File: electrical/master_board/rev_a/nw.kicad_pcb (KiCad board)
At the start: 2 copper layers, 42.2 x 39 mm, 1 part, among them CN70 HCSR04;F1x4H

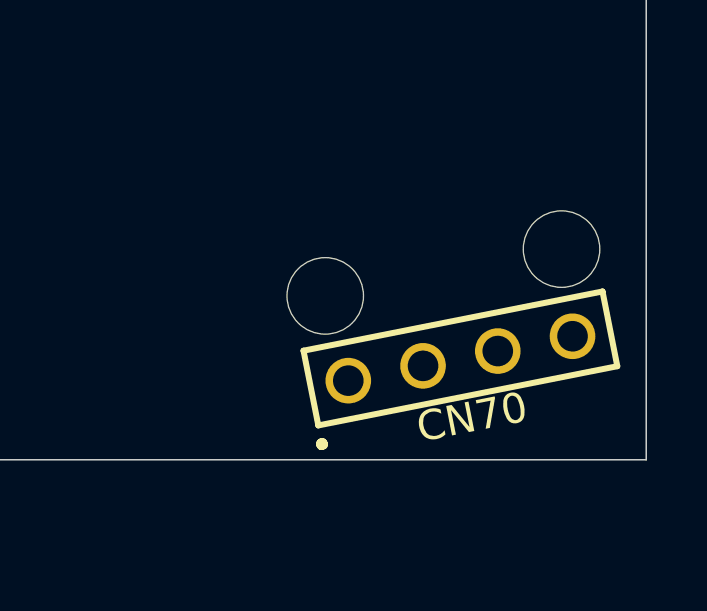
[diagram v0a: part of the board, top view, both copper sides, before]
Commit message: The PCBChunk'ification of Sonars is complete.
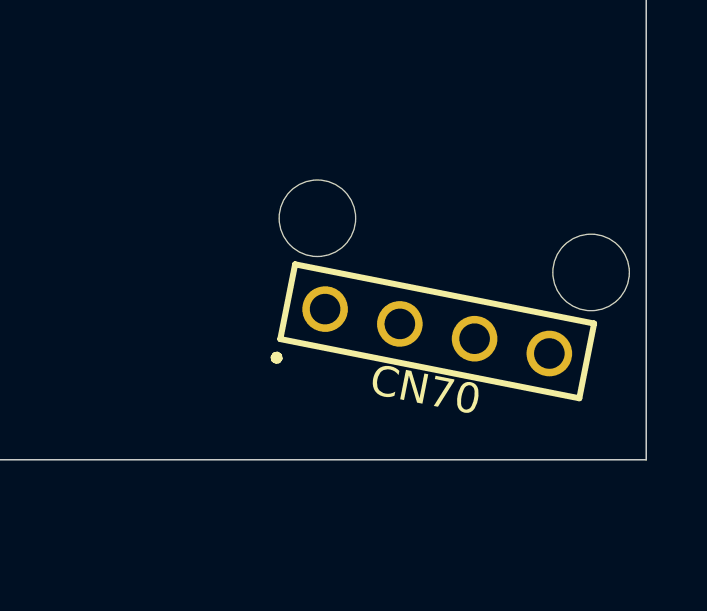
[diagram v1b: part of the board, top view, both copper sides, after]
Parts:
- CN70: value HCSR04;F1x4H -> HCSR04H;F1X4
- moved CN70 1.19 mm to (63.0, 56.7), turned to 168.8 degrees
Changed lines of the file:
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@@
   )
   (module HR2:HCSR04_F1x4H (layer F.Cu)
-    (at 63.8063 57.6226 191.2)
-    (fp_text reference CN70 (at 0 -2 11.2) (layer F.SilkS)
+    (at 63.0334 56.7177 168.8)
+    (fp_text reference CN70 (at 0 -2 168.8) (layer F.SilkS)
       (effects (font (size 1 1) (thickness 0.2)))
     )
-    (fp_text value HCSR04;F1x4H (at 0 0 11.2) (layer F.Fab)
+    (fp_text value HCSR04H;F1X4 (at 0 0 168.8) (layer F.Fab)
       (effects (font (size 1 1) (thickness 0.2)))
     )
@@
     (fp_line (start -5.08 1.27) (end -5.08 -1.27) (layer F.SilkS) (width 0.2))
     (fp_line (start -5.08 -1.27) (end 5.08 -1.27) (layer F.SilkS) (width 0.2))
-    (pad "HCSR04 West Tie Down Hole (High)" np_thru_hole circle (at -4.015 2.921 191.2) (size 2.55 2.55) (drill 2.55) (layers *.Cu *.Mask))
-    (pad "HCSR04 East Tie Down Hole (Hight)" np_thru_hole circle (at 4.015 2.921 191.2) (size 2.55 2.55) (drill 2.55) (layers *.Cu *.Mask))
-    (pad 4 thru_hole circle (at -3.81 0 191.2) (size 1.52 1.52) (drill 1.02) (layers *.Cu *.Mask))
-    (pad 3 thru_hole circle (at -1.27 0 191.2) (size 1.52 1.52) (drill 1.02) (layers *.Cu *.Mask))
-    (pad 2 thru_hole circle (at 1.27 0 191.2) (size 1.52 1.52) (drill 1.02) (layers *.Cu *.Mask))
-    (pad 1 thru_hole circle (at 3.81 0 191.2) (size 1.52 1.52) (drill 1.02) (layers *.Cu *.Mask))
+    (pad "HCSR04 West Tie Down Hole (High)" np_thru_hole circle (at -4.65 2.921 168.8) (size 2.55 2.55) (drill 2.55) (layers *.Cu *.Mask))
+    (pad "HCSR04 East Tie Down Hole (Hight)" np_thru_hole circle (at 4.65 2.921 168.8) (size 2.55 2.55) (drill 2.55) (layers *.Cu *.Mask))
+    (pad 4 thru_hole circle (at -3.81 0 168.8) (size 1.52 1.52) (drill 1.02) (layers *.Cu *.Mask))
+    (pad 3 thru_hole circle (at -1.27 0 168.8) (size 1.52 1.52) (drill 1.02) (layers *.Cu *.Mask))
+    (pad 2 thru_hole circle (at 1.27 0 168.8) (size 1.52 1.52) (drill 1.02) (layers *.Cu *.Mask))
+    (pad 1 thru_hole circle (at 3.81 0 168.8) (size 1.52 1.52) (drill 1.02) (layers *.Cu *.Mask))
   )
   (gr_line (start 70 61) (end 70 26.46) (layer Edge.Cuts) (width 0.05))

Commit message: Finally have everything fitting together.
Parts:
- moved CN70 3.97 mm to (61.9, 60.5)
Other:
- outline, holes or cut-outs redrawn
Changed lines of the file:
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@@
   )
   (module HR2:HCSR04_F1x4H (layer F.Cu)
-    (at 63.0334 56.7177 168.8)
+    (at 61.8716 60.5169 168.8)
     (fp_text reference CN70 (at 0 -2 168.8) (layer F.SilkS)
       (effects (font (size 1 1) (thickness 0.2)))
@@
     (pad 1 thru_hole circle (at 3.81 0 168.8) (size 1.52 1.52) (drill 1.02) (layers *.Cu *.Mask))
   )
-  (gr_line (start 70 61) (end 70 26.46) (layer Edge.Cuts) (width 0.05))
+  (gr_line (start 70 61.5) (end 70 26.46) (layer Edge.Cuts) (width 0.05))
   (gr_line (start 70 26.46) (end 69.99 26.33) (layer Edge.Cuts) (width 0.05))
   (gr_line (start 69.99 26.33) (end 69.98 26.19) (layer Edge.Cuts) (width 0.05))
@@
   (gr_line (start 29.2 63.99) (end 29.33 64) (layer Edge.Cuts) (width 0.05))
   (gr_line (start 29.33 64) (end 37.5 64) (layer Edge.Cuts) (width 0.05))
-  (gr_line (start 37.5 64) (end 37.5 62.5) (layer Edge.Cuts) (width 0.05))
-  (gr_line (start 37.5 62.5) (end 37.51 62.37) (layer Edge.Cuts) (width 0.05))
-  (gr_line (start 37.51 62.37) (end 37.52 62.24) (layer Edge.Cuts) (width 0.05))
-  (gr_line (start 37.52 62.24) (end 37.55 62.11) (layer Edge.Cuts) (width 0.05))
-  (gr_line (start 37.55 62.11) (end 37.59 61.99) (layer Edge.Cuts) (width 0.05))
-  (gr_line (start 37.59 61.99) (end 37.64 61.87) (layer Edge.Cuts) (width 0.05))
-  (gr_line (start 37.64 61.87) (end 37.7 61.75) (layer Edge.Cuts) (width 0.05))
-  (gr_line (start 37.7 61.75) (end 37.77 61.64) (layer Edge.Cuts) (width 0.05))
-  (gr_line (start 37.77 61.64) (end 37.85 61.54) (layer Edge.Cuts) (width 0.05))
-  (gr_line (start 37.85 61.54) (end 37.94 61.44) (layer Edge.Cuts) (width 0.05))
-  (gr_line (start 37.94 61.44) (end 38.04 61.35) (layer Edge.Cuts) (width 0.05))
-  (gr_line (start 38.04 61.35) (end 38.14 61.27) (layer Edge.Cuts) (width 0.05))
-  (gr_line (start 38.14 61.27) (end 38.25 61.2) (layer Edge.Cuts) (width 0.05))
-  (gr_line (start 38.25 61.2) (end 38.37 61.14) (layer Edge.Cuts) (width 0.05))
-  (gr_line (start 38.37 61.14) (end 38.49 61.09) (layer Edge.Cuts) (width 0.05))
-  (gr_line (start 38.49 61.09) (end 38.61 61.05) (layer Edge.Cuts) (width 0.05))
-  (gr_line (start 38.61 61.05) (end 38.74 61.02) (layer Edge.Cuts) (width 0.05))
-  (gr_line (start 38.74 61.02) (end 38.87 61.01) (layer Edge.Cuts) (width 0.05))
-  (gr_line (start 38.87 61.01) (end 39 61) (layer Edge.Cuts) (width 0.05))
-  (gr_line (start 39 61) (end 70 61) (layer Edge.Cuts) (width 0.05))
+  (gr_line (start 37.5 64) (end 37.5 63) (layer Edge.Cuts) (width 0.05))
+  (gr_line (start 37.5 63) (end 37.51 62.87) (layer Edge.Cuts) (width 0.05))
+  (gr_line (start 37.51 62.87) (end 37.52 62.74) (layer Edge.Cuts) (width 0.05))
+  (gr_line (start 37.52 62.74) (end 37.55 62.61) (layer Edge.Cuts) (width 0.05))
+  (gr_line (start 37.55 62.61) (end 37.59 62.49) (layer Edge.Cuts) (width 0.05))
+  (gr_line (start 37.59 62.49) (end 37.64 62.37) (layer Edge.Cuts) (width 0.05))
+  (gr_line (start 37.64 62.37) (end 37.7 62.25) (layer Edge.Cuts) (width 0.05))
+  (gr_line (start 37.7 62.25) (end 37.77 62.14) (layer Edge.Cuts) (width 0.05))
+  (gr_line (start 37.77 62.14) (end 37.85 62.04) (layer Edge.Cuts) (width 0.05))
+  (gr_line (start 37.85 62.04) (end 37.94 61.94) (layer Edge.Cuts) (width 0.05))
+  (gr_line (start 37.94 61.94) (end 38.04 61.85) (layer Edge.Cuts) (width 0.05))
+  (gr_line (start 38.04 61.85) (end 38.14 61.77) (layer Edge.Cuts) (width 0.05))
+  (gr_line (start 38.14 61.77) (end 38.25 61.7) (layer Edge.Cuts) (width 0.05))
+  (gr_line (start 38.25 61.7) (end 38.37 61.64) (layer Edge.Cuts) (width 0.05))
+  (gr_line (start 38.37 61.64) (end 38.49 61.59) (layer Edge.Cuts) (width 0.05))
+  (gr_line (start 38.49 61.59) (end 38.61 61.55) (layer Edge.Cuts) (width 0.05))
+  (gr_line (start 38.61 61.55) (end 38.74 61.52) (layer Edge.Cuts) (width 0.05))
+  (gr_line (start 38.74 61.52) (end 38.87 61.51) (layer Edge.Cuts) (width 0.05))
+  (gr_line (start 38.87 61.51) (end 39 61.5) (layer Edge.Cuts) (width 0.05))
+  (gr_line (start 39 61.5) (end 70 61.5) (layer Edge.Cuts) (width 0.05))
 )

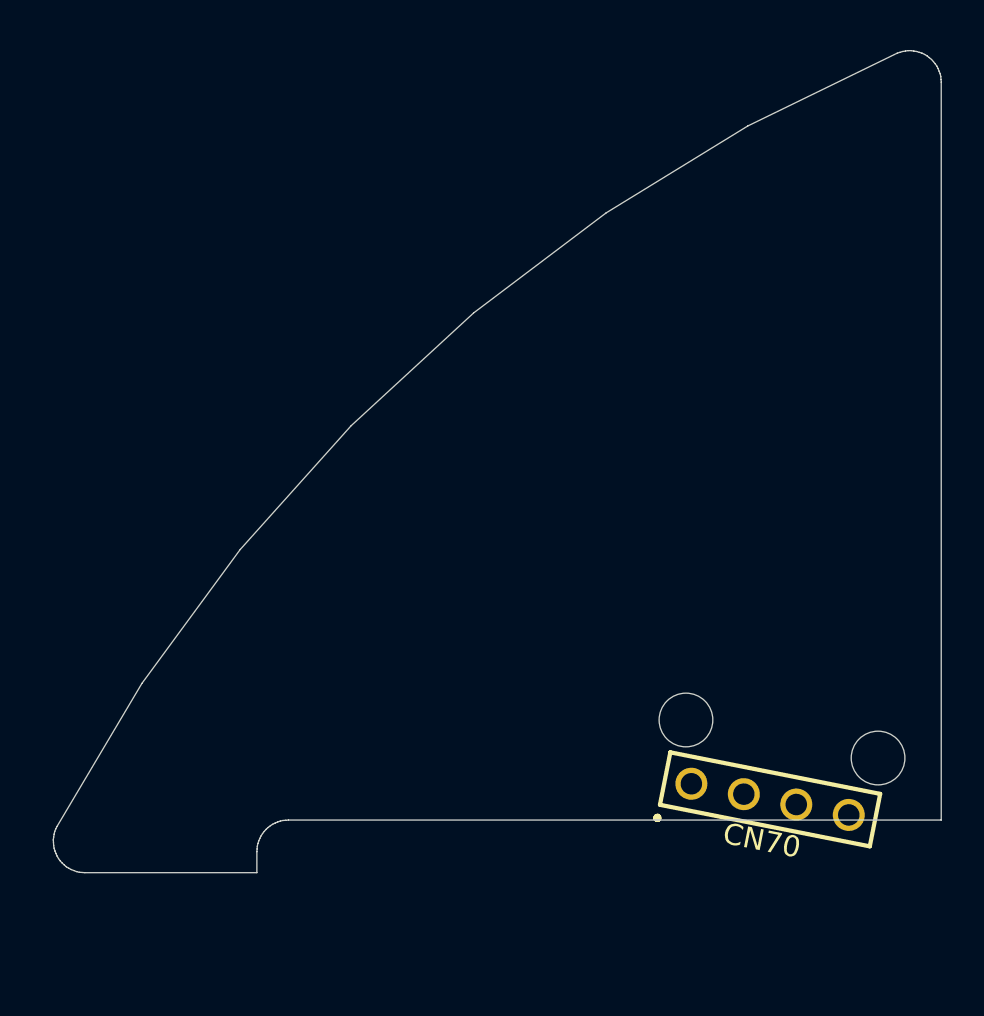
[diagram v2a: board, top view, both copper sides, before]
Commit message: Added spacer mounting holes to schematics and associated PCB's.
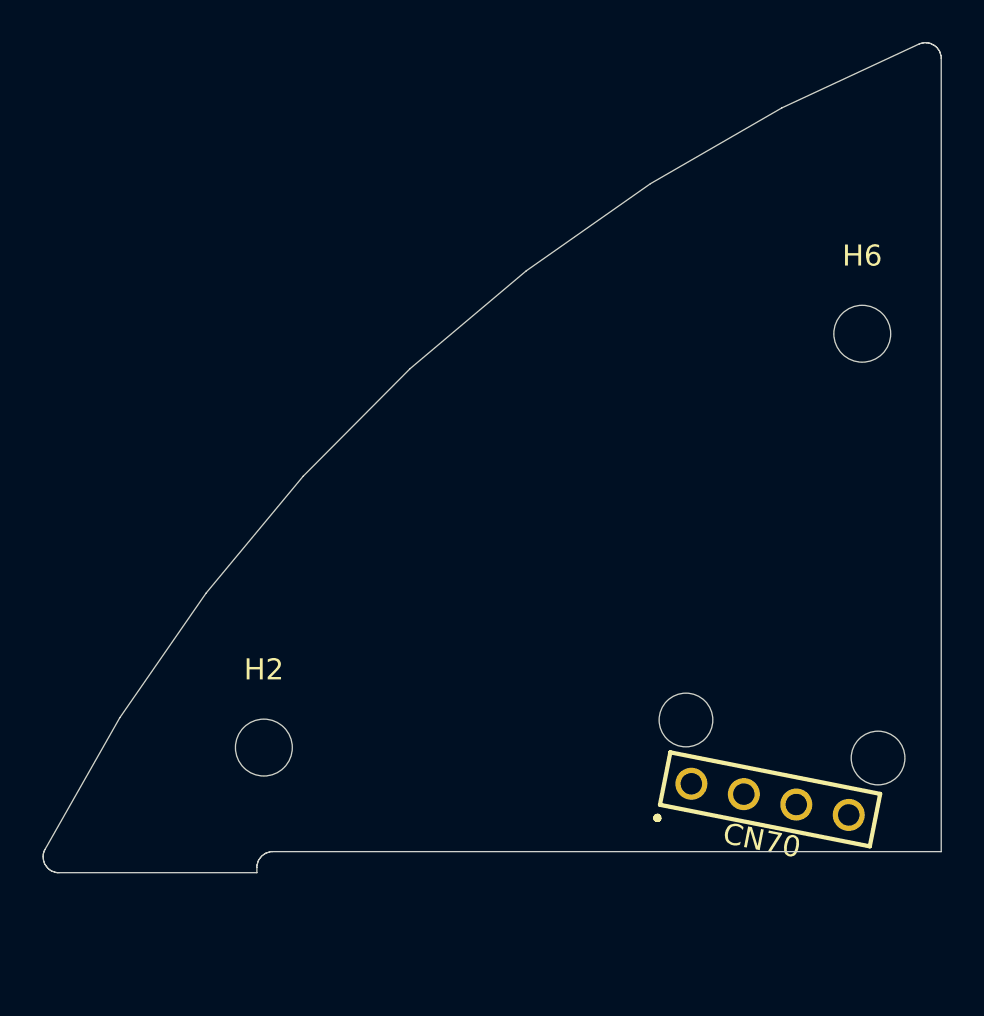
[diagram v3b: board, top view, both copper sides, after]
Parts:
- added H2: HOLE;M2.5, MountingHole:MountingHole_2.7mm_M2.5, F.Cu at (37.8, 58.1)
- added H6: HOLE;M2.5, MountingHole:MountingHole_2.7mm_M2.5, F.Cu at (66.2, 38.4)
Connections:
- CN70 pad 1: (no net) -> Net-(CN70-Pad1)
- CN70 pad 2: (no net) -> Net-(CN70-Pad2)
- CN70 pad 3: (no net) -> Net-(CN70-Pad3)
- CN70 pad 4: (no net) -> Net-(CN70-Pad4)
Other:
- board size 42.2 x 39 mm -> 42.6 x 39.4 mm

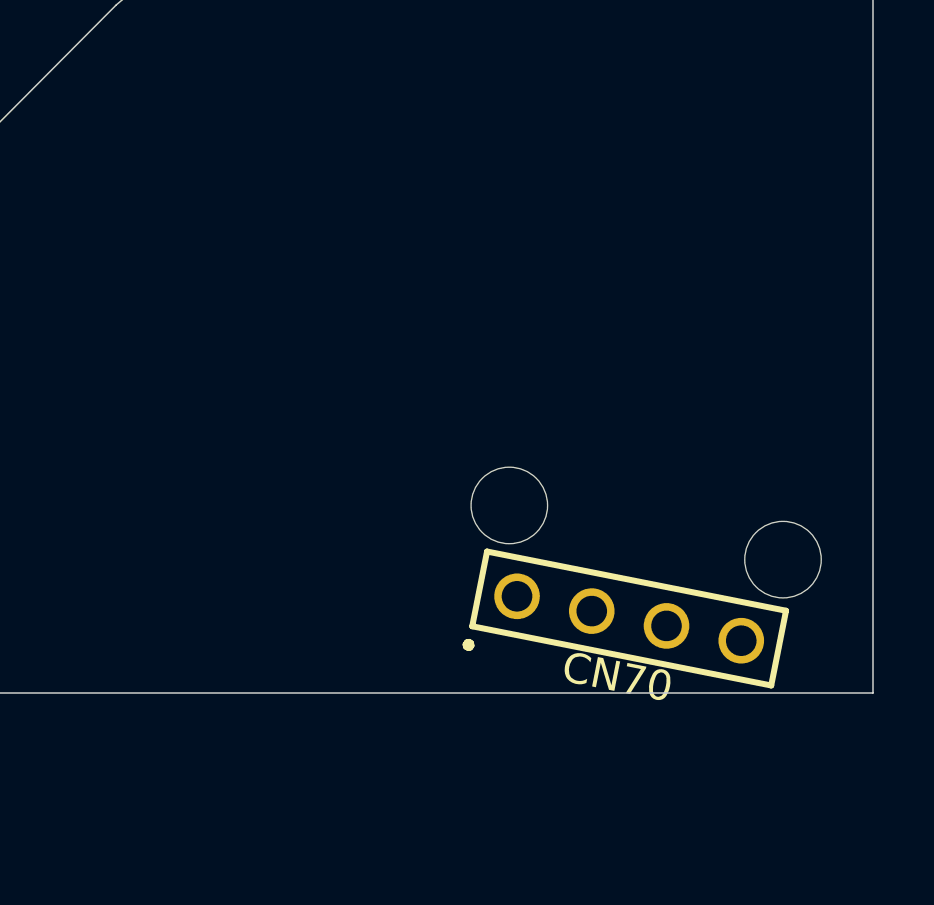
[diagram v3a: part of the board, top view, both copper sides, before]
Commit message: Placed all of the Groves on the PCB's.
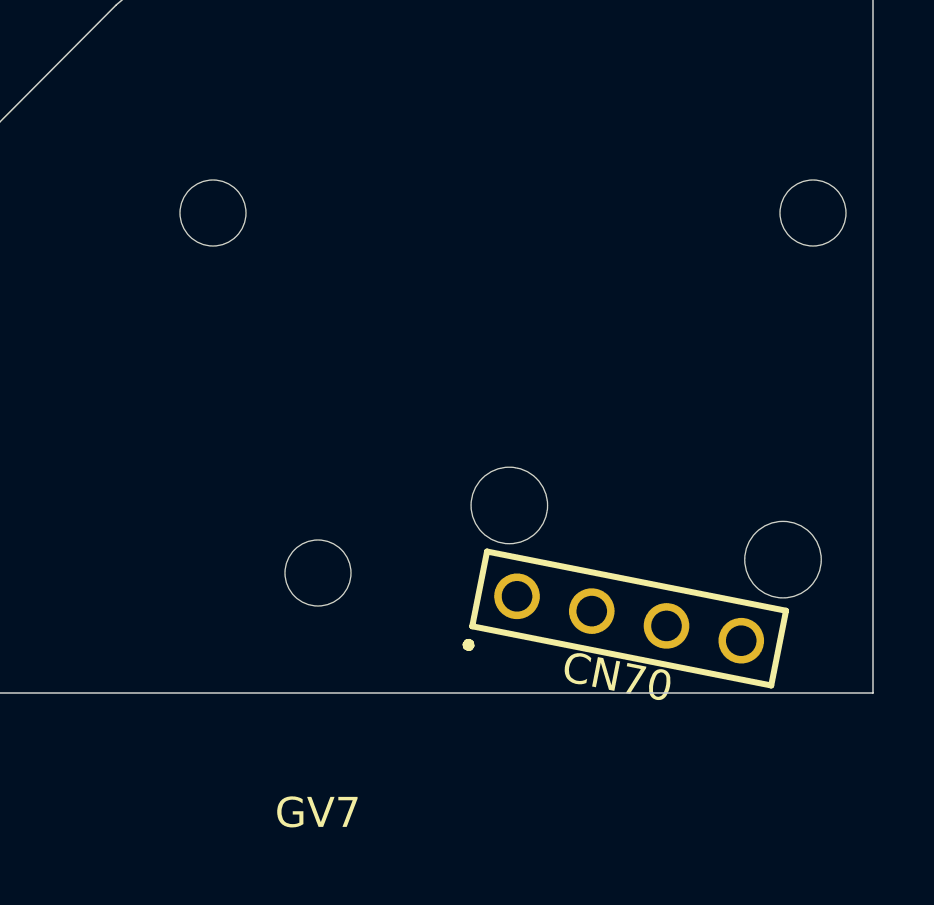
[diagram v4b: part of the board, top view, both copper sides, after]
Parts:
- added GV1: GROVE;20x20, HR2:GROVE20x20, B.Cu at (58.0, 47.0)
- added GV7: GROVE;20x20R, HR2:GROVE20x20R, F.Cu at (51.5, 69.0)

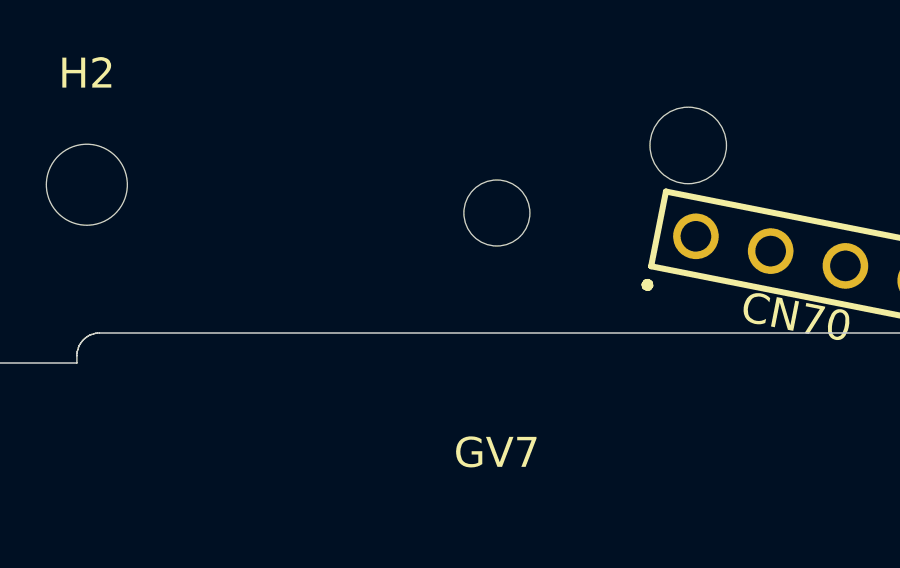
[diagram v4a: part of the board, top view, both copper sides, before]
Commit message: Fixed Groves and added MikroBus's.
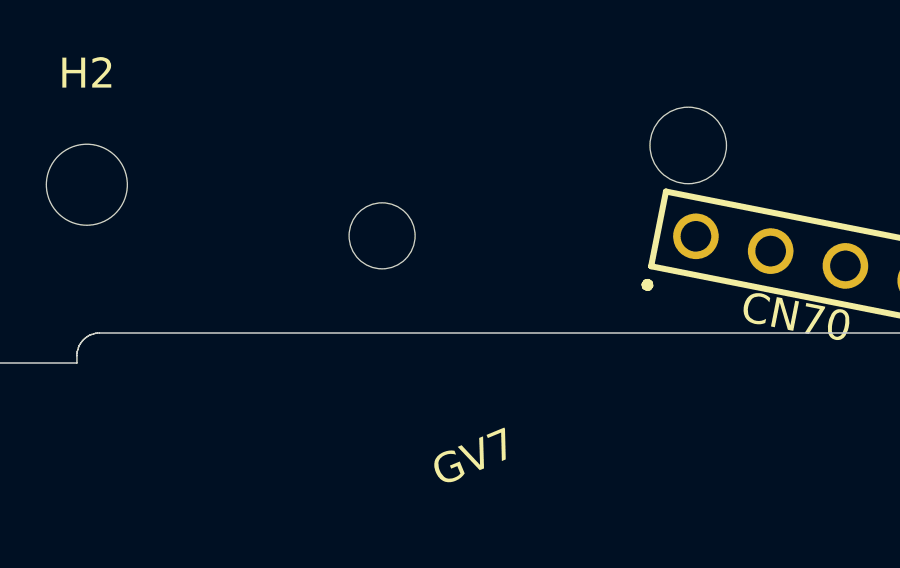
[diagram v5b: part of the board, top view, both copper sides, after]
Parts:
- turned GV7 to 22.5 degrees
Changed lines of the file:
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@@
   )
   (module HR2:GROVE20x20R (layer F.Cu)
-    (at 51.5 69)
-    (fp_text reference GV7 (at 0 -2) (layer F.SilkS)
+    (at 51.5 69 22.5)
+    (fp_text reference GV7 (at 0 -2 22.5) (layer F.SilkS)
       (effects (font (size 1 1) (thickness 0.2)))
     )
-    (fp_text value GROVE;20x20R (at 0 0) (layer F.Fab)
+    (fp_text value GROVE;20x20R (at 0 0 22.5) (layer F.Fab)
       (effects (font (size 1 1) (thickness 0.2)))
     )
-    (pad "N[0] Blue 20x20 Grove" np_thru_hole circle (at 0 -10) (size 2.2 2.2) (drill 2.2) (layers *.Cu *.Mask))
+    (pad "N[0] Blue 20x20 Grove" np_thru_hole circle (at 0 -10 22.5) (size 2.2 2.2) (drill 2.2) (layers *.Cu *.Mask))
   )
   (module HR2:GROVE20x20 (layer B.Cu)
